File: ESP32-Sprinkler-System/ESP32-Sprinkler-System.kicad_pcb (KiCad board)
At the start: 2 copper layers, 120 x 120 mm, 66 parts, among them J101 12V, J102 DHT, J103 NEOPIXEL, J104 LCD, J105 BME280, J201 TBL004-508-02BE-2GY, J202 TBL004-508-02BE-2GY, J203 TBL004-508-02BE-2GY, J204 TBL004-508-02BE-2GY, Q201 IRFZ24NPBF, Q202 IRFZ24NPBF, Q203 IRFZ24NPBF, Q204 IRFZ24NPBF, U101 V7805-500, U102 ESP32-DEVKITC-32D, U201 MC33152PG, U202 MC33152PG

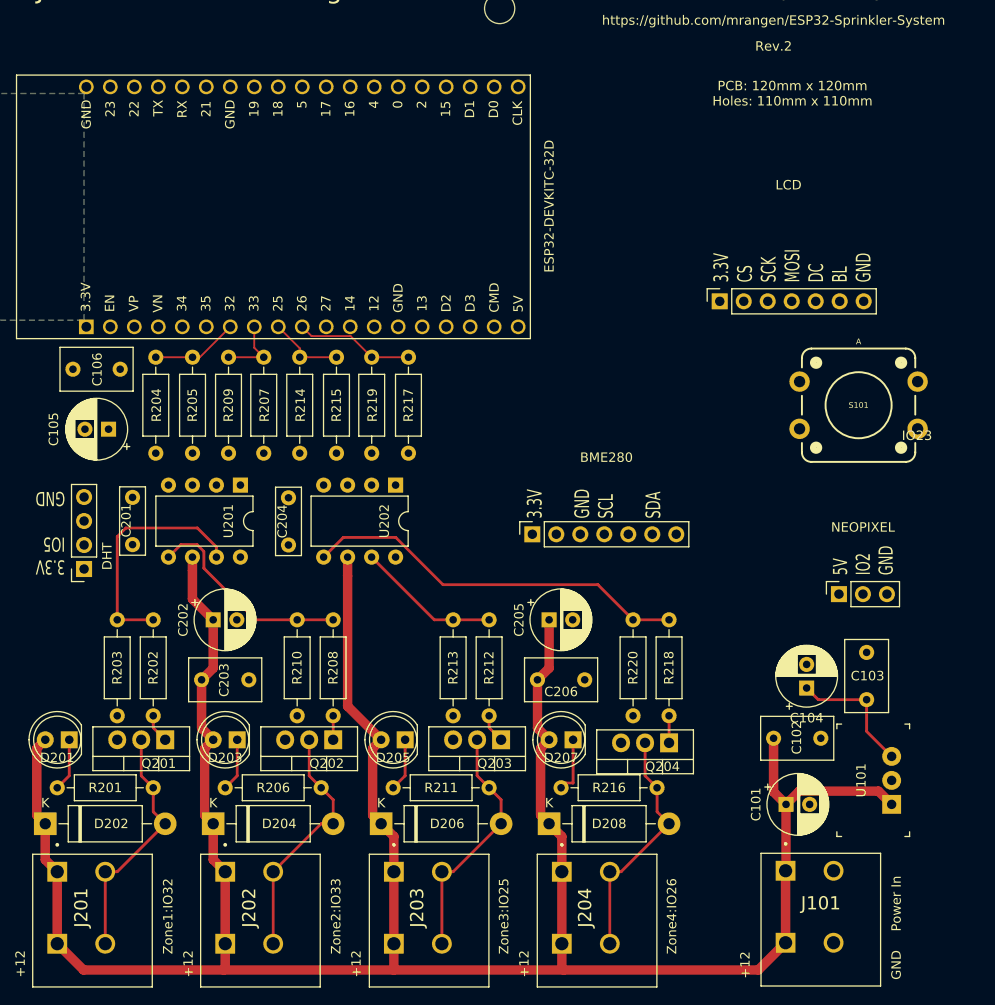
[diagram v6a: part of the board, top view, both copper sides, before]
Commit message: finished fixes and trace placement.
mike needs to review
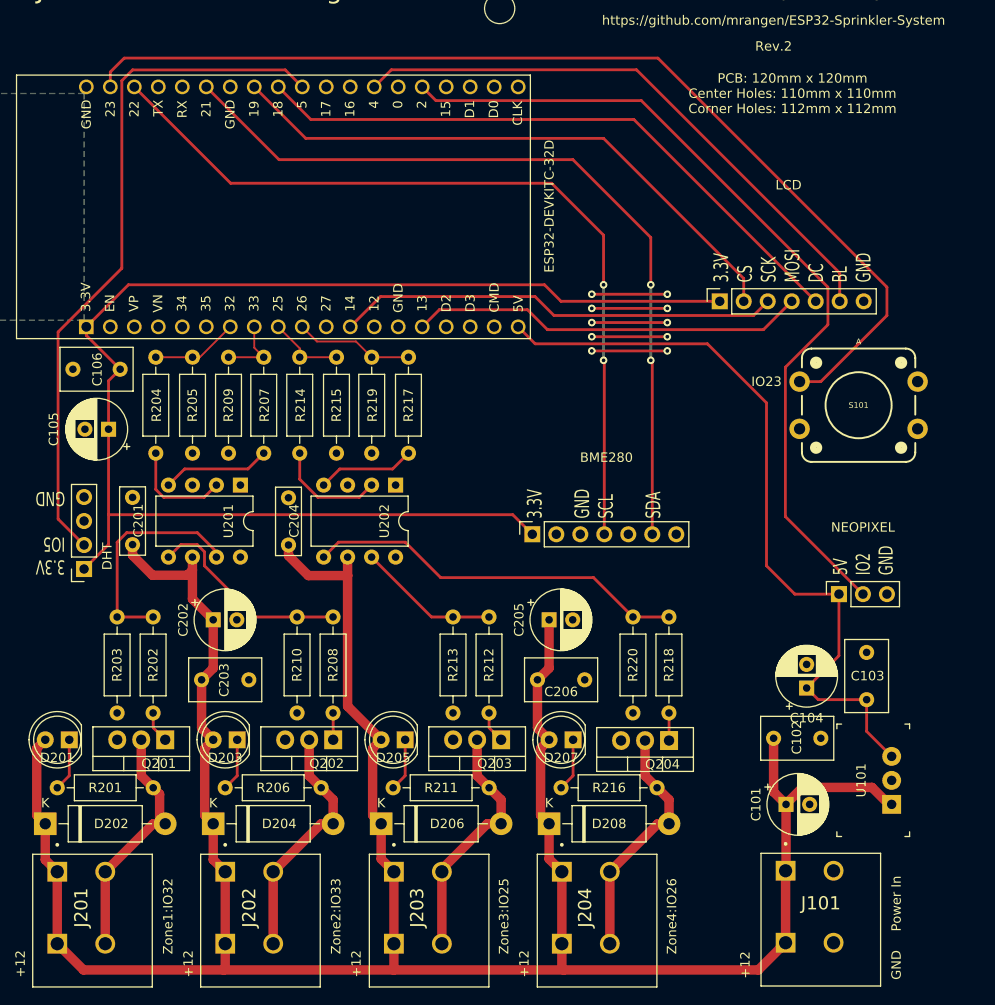
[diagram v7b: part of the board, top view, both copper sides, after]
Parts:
- moved R208 0.30 mm to (121.4, 106.4)
- moved R210 0.30 mm to (117.5, 106.4)
- moved R212 0.30 mm to (137.9, 106.4)
- moved R213 0.30 mm to (134.1, 106.4)
- moved R218 0.30 mm to (156.9, 106.4)
- moved R202 0.30 mm to (102.3, 106.4)
- moved R203 0.30 mm to (98.5, 106.4)
- moved R220 0.30 mm to (153.1, 106.4)
- moved Q204 0.25 mm to (156.9, 119.5)
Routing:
- net 3.3V: track 0.00 -> 144.1 mm
- net SW_A: track 0.00 -> 109.6 mm
- net NEOPIXEL: track 0.00 -> 89.5 mm
- net SCL: track 0.00 -> 87.9 mm, vias 0 -> 2
- net SDA: track 0.00 -> 85.1 mm, vias 0 -> 2
- net DHT: track 0.00 -> 73.4 mm
- net 5V: track 14.0 -> 81.1 mm
- net D/C: track 0.00 -> 66.3 mm
- net CS: track 0.00 -> 62.6 mm
- net BACKLIGHT: track 0.00 -> 61.9 mm
- net SCK: track 0.00 -> 47.0 mm
- net MOSI: track 0.00 -> 42.0 mm
- net GND: track 0.00 -> 40.0 mm, vias 0 -> 10
- net 12V: track 269.6 -> 286.8 mm
- net Net-(R214-Pad2): track 0.00 -> 11.7 mm
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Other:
- board text added: "PCB: 120mm x 120mm Center Holes: 110mm x 110mm Corner Holes: 112mm x 112mm"
- board text removed: "PCB: 120mm x 120mm Holes: 110mm x 110mm"
